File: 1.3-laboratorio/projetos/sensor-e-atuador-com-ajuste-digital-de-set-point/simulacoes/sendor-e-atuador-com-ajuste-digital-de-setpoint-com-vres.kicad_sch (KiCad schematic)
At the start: 30 parts, among them U1 OPAMP, U2 OPAMP, U3 OPAMP

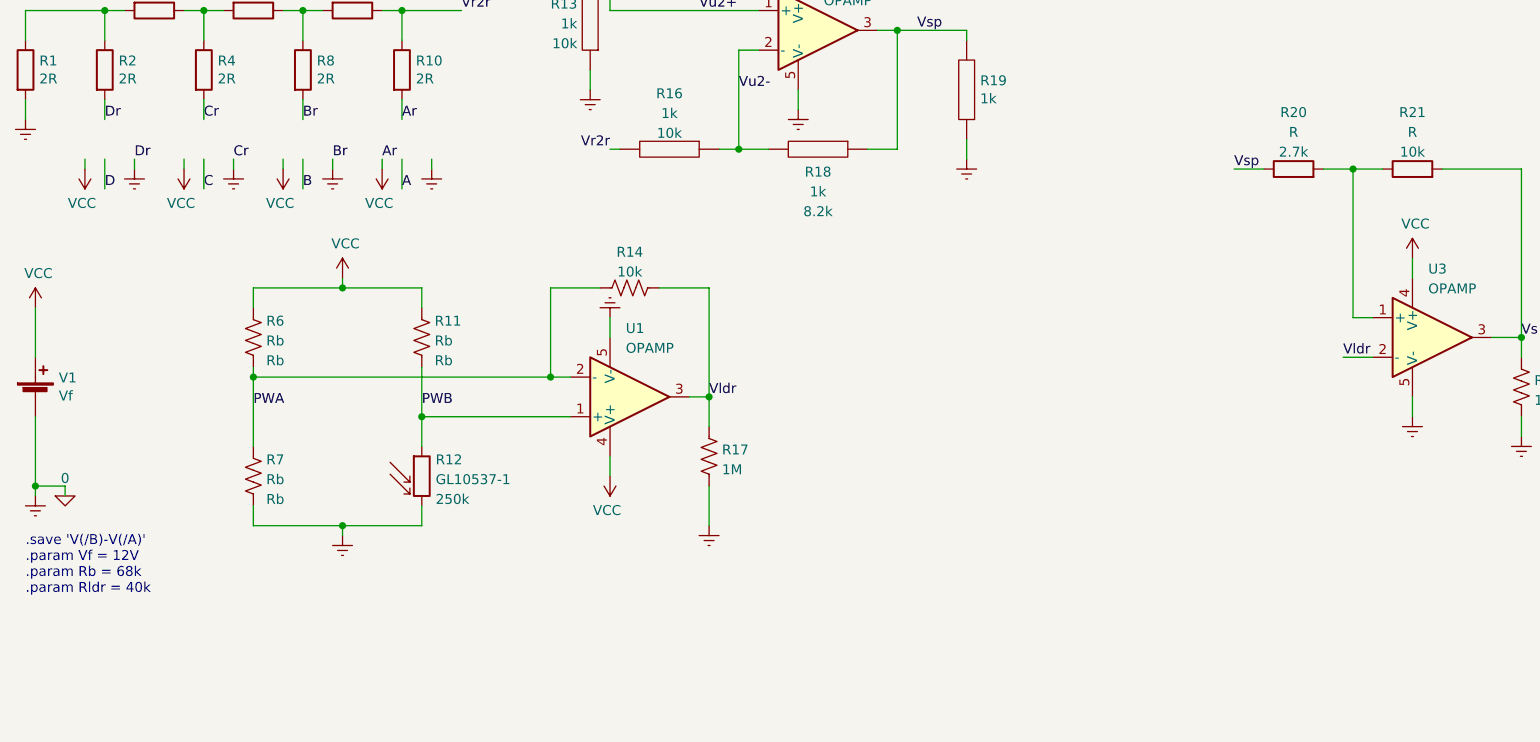
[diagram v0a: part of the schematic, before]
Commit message: Estudos e simulações para o projeto sensor-e-atuador-com-ajuste-digital-de-set-point.
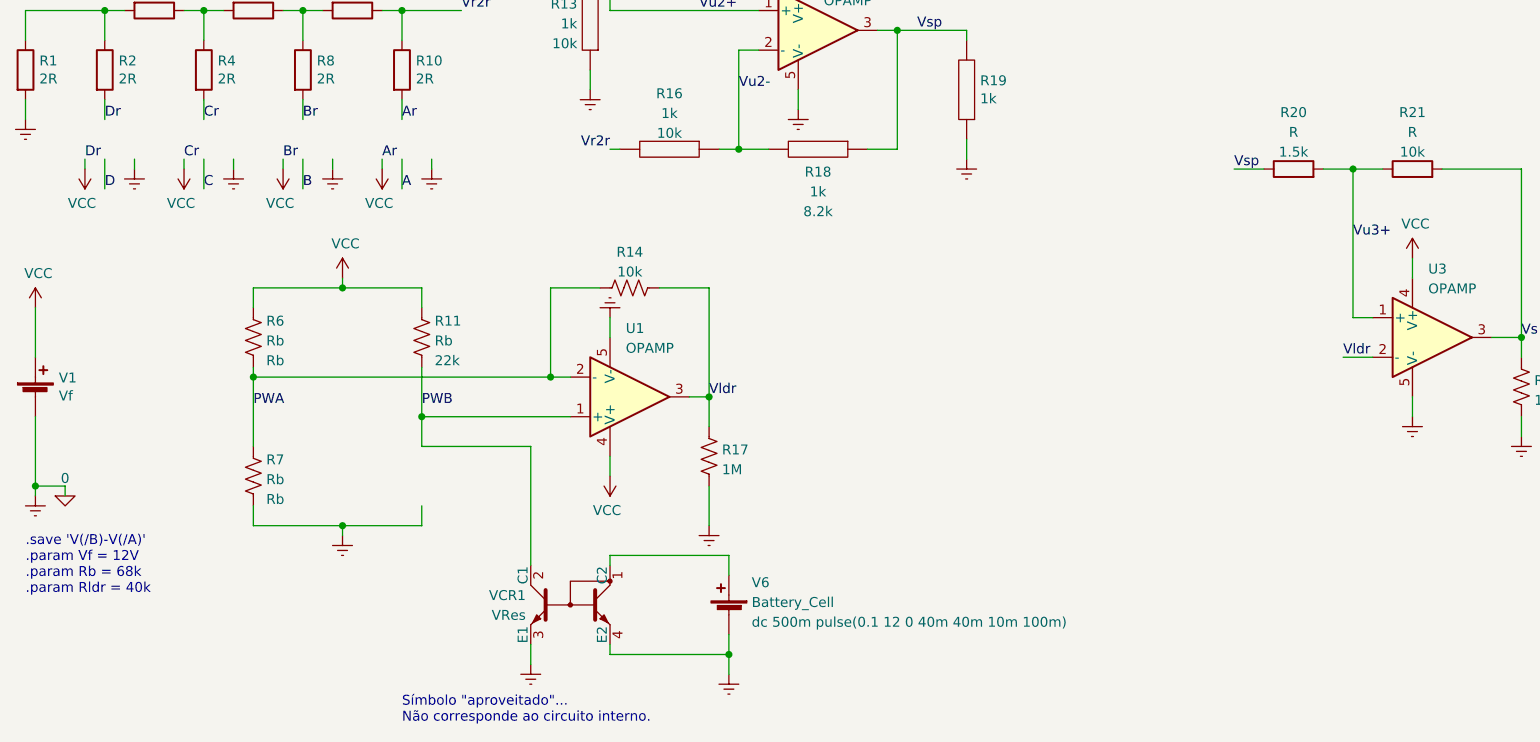
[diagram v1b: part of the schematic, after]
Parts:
- removed R12: GL10537-1, symbol ldr-ponte-rescue:R_PHOTO-Device
- added V6: Battery_Cell, symbol Device:Battery_Cell
- added VCR1: VRes, symbol Device:Q_Dual_NPN_C2C1E1E2
- R11: Spice_Model Rb -> 22k
- R20: Spice_Model 2.7k -> 1.5k
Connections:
- net 0: now also V6.2 (-), VCR1.3 (E1), VCR1.4 (E2); no longer R2.2, R4.2, R8.2
- net PWB: now also VCR1.2 (C1)
- net VCC: now also R2.2, R4.2, R8.2
- net Vu3+: now reaches R20.2, R21.1, U3.1 (+)
- new net: V6.1 (+), VCR1.1 (C2)
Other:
- note added: "Símbolo "aproveitado"... Não corresponde ao circuito interno."

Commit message: Desenho final do projeto sensor-e-atuador-com-ajuste-digital-de-set-point em andamento.
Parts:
- R1, R10, R2, R4, R8: Spice_Model 2.2k -> 22k
- R12: renamed from R13; Spice_Model 10k -> 100k
- R14: renamed from R15; Spice_Model 10k -> 100k
- R15: renamed from R16; Spice_Model 10k -> 100k
- R17: renamed from R18; Spice_Model 8.2k -> 82k
- R18: renamed from R19; value 1k -> 10k
- R3, R5, R9: Spice_Model 1.1k -> 11k
- V6: Spice_Model dc 500m pulse(0.1 12 0 40m 40m 10m 100m) -> dc 500m pulse(0 20 0 40m 40m 10m 100m)
- renumbered R14 to R13, R17 to R16, R20 to R19, R21 to R20, R22 to R21
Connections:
- net 0: now also R11.1, R6.1; no longer R7.2, VCR1.3 (E1)
- net VCC: now also R7.2, VCR1.3 (E1); no longer R11.1, R6.1
- net Vctrl: now reaches V6.1 (+), VCR1.1 (C2)
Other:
- moved on the sheet: R19, R20, R21, U3

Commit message: Versão preliminar do projeto.
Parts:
- R12: Spice_Model 100k -> 120k
- R14: Spice_Model 100k -> 220k
- R17: Spice_Model 82k -> 160k
- V2: Spice_Model dc Vf pulse(0 Vf 50m ts td 50m 100m) -> dc Vf pwl(0 0 50m 0 '50m+ts' Vf 62.5m Vf '62.5m+td' 0 r =0)
- V3: Spice_Model dc Vf pulse(0 Vf 25m ts td 25m 50m) -> dc Vf pwl(0 0 25m 0 '25m+ts' Vf 50m Vf '50m+td' 0 62.5m 0 r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
- V4: Spice_Model dc Vf pulse(0 Vf 12.5m ts td 12.5m 25m) -> dc Vf pwl(0 0 12.5m 0 '12.5m+ts' Vf 25m Vf '25m+td' 0 37.5m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
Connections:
- net A: now also R10.2
- net B: now also R8.2
- net C: now also R4.2
- net D: now also R2.2
- net VCC: no longer R10.2, R2.2, R4.2, R8.2
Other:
- moved on the sheet: V3, V4, V5

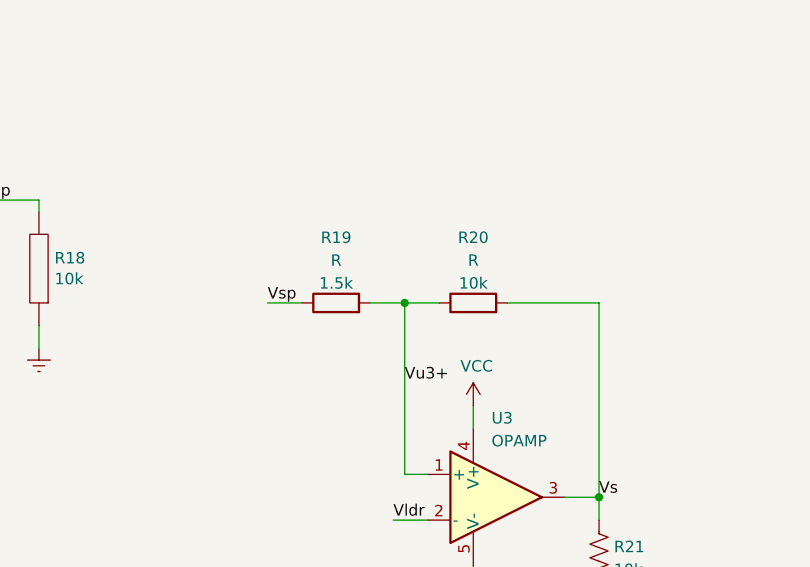
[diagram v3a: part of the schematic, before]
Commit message: Teste em protoboard realizado e ajustes realizados no esquemático. Projeto concluído.
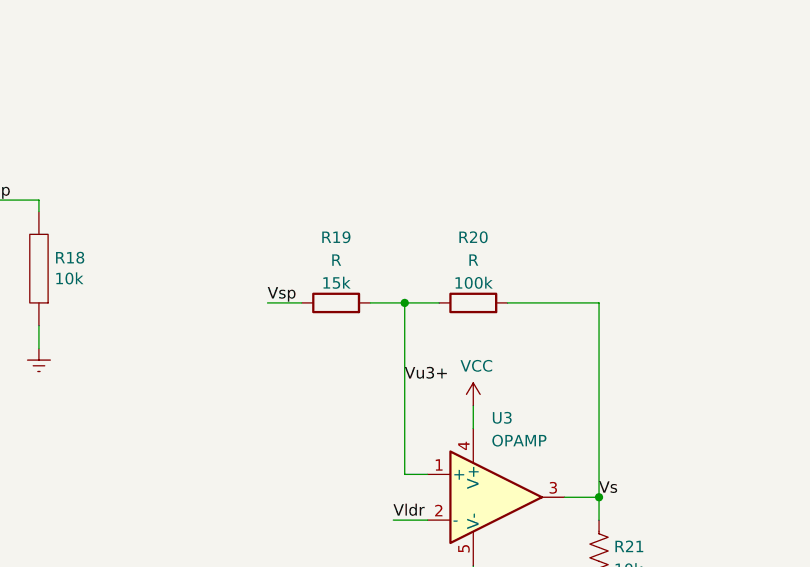
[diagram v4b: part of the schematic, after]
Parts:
- R19: Spice_Model 1.5k -> 15k
- R20: Spice_Model 10k -> 100k
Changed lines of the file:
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@@
       (effects (font (size 1.27 1.27)) hide)
     )
-    (property "Spice_Model" "1.5k" (id 6) (at 176.53 98.1512 90))
+    (property "Spice_Model" "15k" (id 6) (at 176.53 98.1512 90))
     (property "Spice_Netlist_Enabled" "Y" (id 7) (at 176.53 100.33 0)
       (effects (font (size 1.27 1.27)) hide)
@@
       (effects (font (size 1.27 1.27)) hide)
     )
-    (property "Spice_Model" "10k" (id 6) (at 191.77 98.1512 90))
+    (property "Spice_Model" "100k" (id 6) (at 191.77 98.1512 90))
     (property "Spice_Netlist_Enabled" "Y" (id 7) (at 191.77 100.33 0)
       (effects (font (size 1.27 1.27)) hide)
